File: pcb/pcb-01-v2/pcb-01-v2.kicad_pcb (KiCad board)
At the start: 4 copper layers, 88 x 64 mm, 166 parts, among them J1 43045-0200 POWER, J2 43650-0300, J3 B3B-PH-K-S(LF)(SN), J4 USB4105-GF-A, Q1 DMP6023LE-13, Q2 2N7002K-7, Q3 2N7002K-7, SW1 PTS645SK43SMTR92LFS, SW2 PTS645SK43SMTR92LFS, SW3 PTS645SK43SMTR92LFS, U1 MCF8316DVRGFR, U10 SN74LVC1G17DCKR, U11 SN74LVC1G17DCKR, U12 TMP1075DGKR, U13 TPD2EUSB30DRTR, U14 TPD2EUSB30DRTR, U2 ESP32-C6-WROOM-1-N8, U3 TPSM365R6V3RDNR, U4 TPS7A1601ADGNR, U5 SN74LVC1G74DCTR, U6 SN74LVC1G74DCTR, U7 TPS3435CAKAGDDFR, U8 LM2907M-14/NOPB, U9 TLV1701AIDBVR

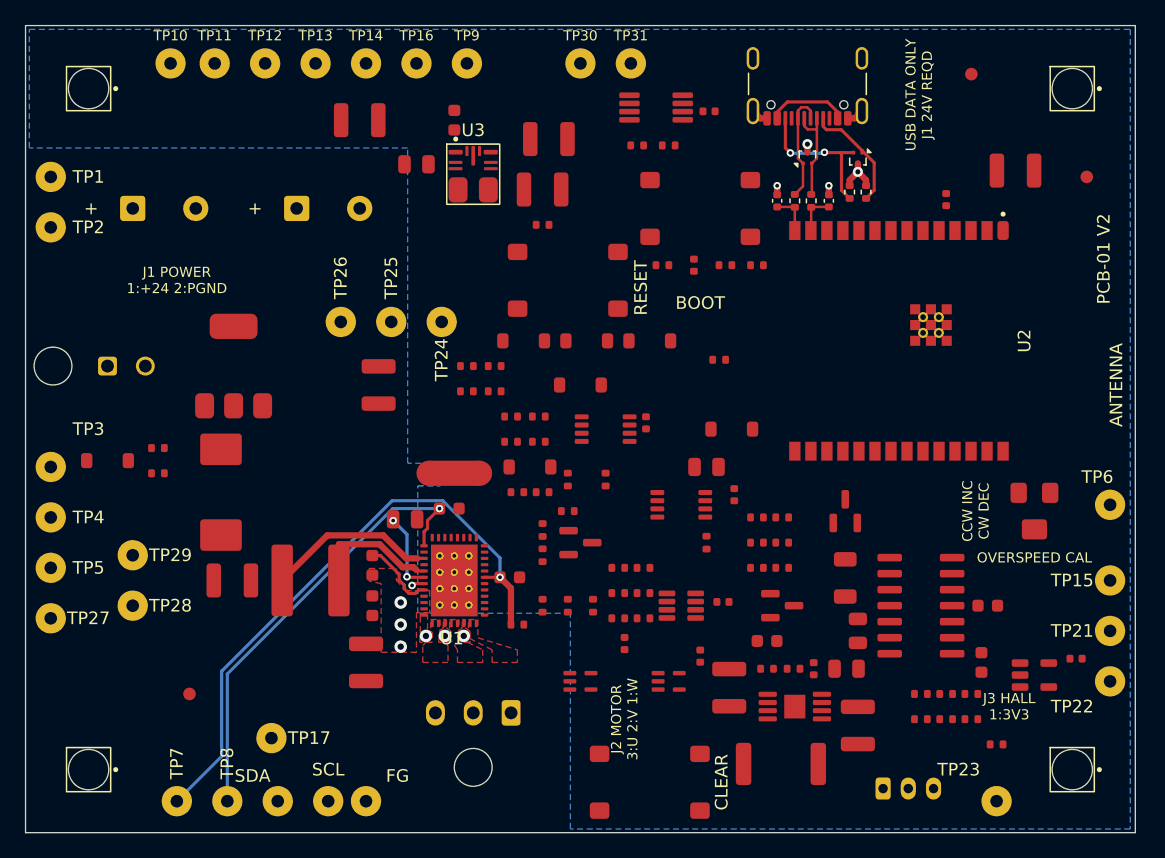
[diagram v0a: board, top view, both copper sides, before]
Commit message: Complete provisional PCB-01 V2 routing
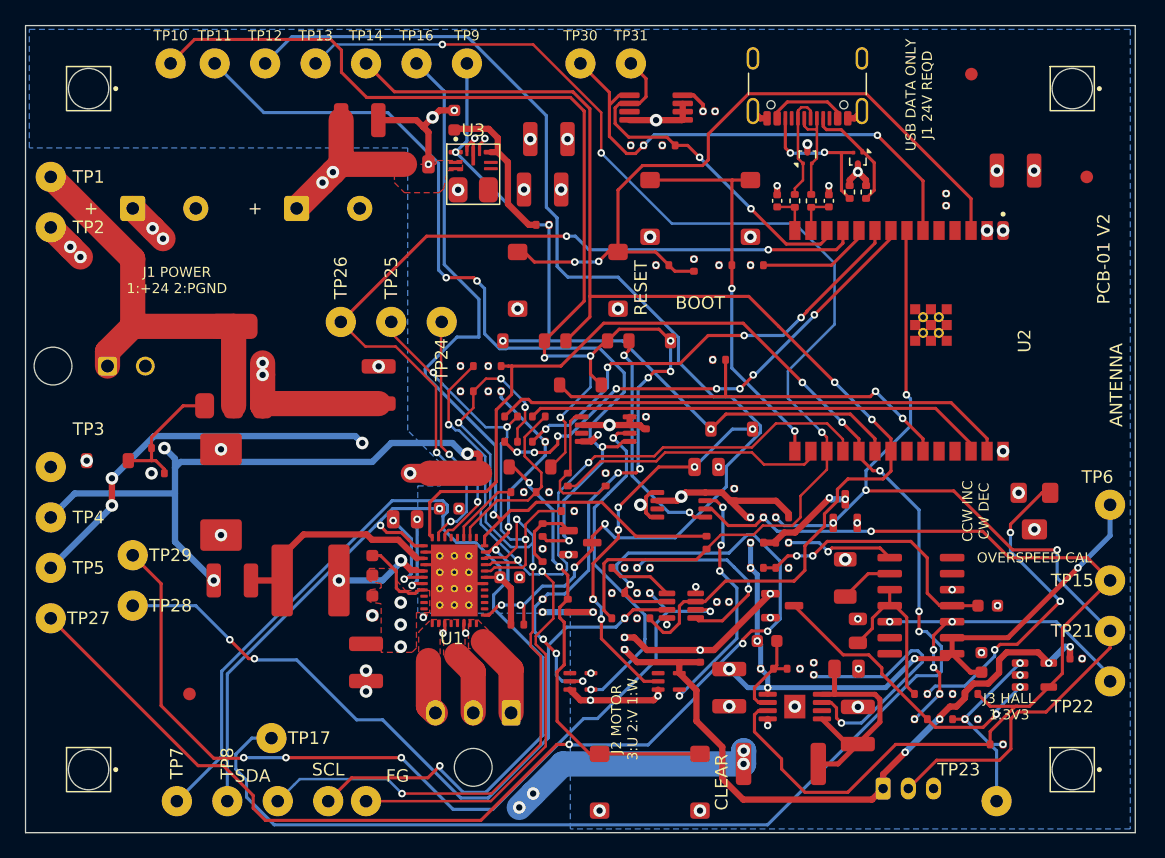
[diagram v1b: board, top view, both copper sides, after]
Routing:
- net NFAULT: track 0.00 -> 142.0 mm, vias 0 -> 5
- net U5_CLR_OR: track 0.00 -> 119.8 mm, vias 0 -> 12
- net 3V3: track 0.00 -> 114.1 mm, vias 0 -> 38
- net AGND: track 8.22 -> 108.4 mm, vias 4 -> 68
- net WD_MR: track 0.00 -> 98.3 mm, vias 0 -> 4
- net WDO: track 0.00 -> 97.5 mm, vias 0 -> 2
- net WD_HEARTBEAT: track 0.00 -> 96.4 mm, vias 0 -> 3
- net DRVOFF: track 0.00 -> 93.8 mm, vias 0 -> 4
- net FG: track 0.00 -> 90.6 mm, vias 0 -> 4
- net OVERSPEED_N: track 0.00 -> 81.4 mm, vias 0 -> 2
- net HALL_TACH: track 0.00 -> 79.5 mm, vias 0 -> 5
- net SDA: track 0.00 -> 73.0 mm, vias 0 -> 6
- net WD_EN: track 0.00 -> 71.3 mm, vias 0 -> 5
- net U5_Q: track 0.00 -> 70.7 mm, vias 0 -> 4
- net ALARM: track 0.00 -> 68.2 mm, vias 0 -> 4
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- removed copper zone on F.Cu, net PGND

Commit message: Finalize PCB-01 V2 JLC submission package
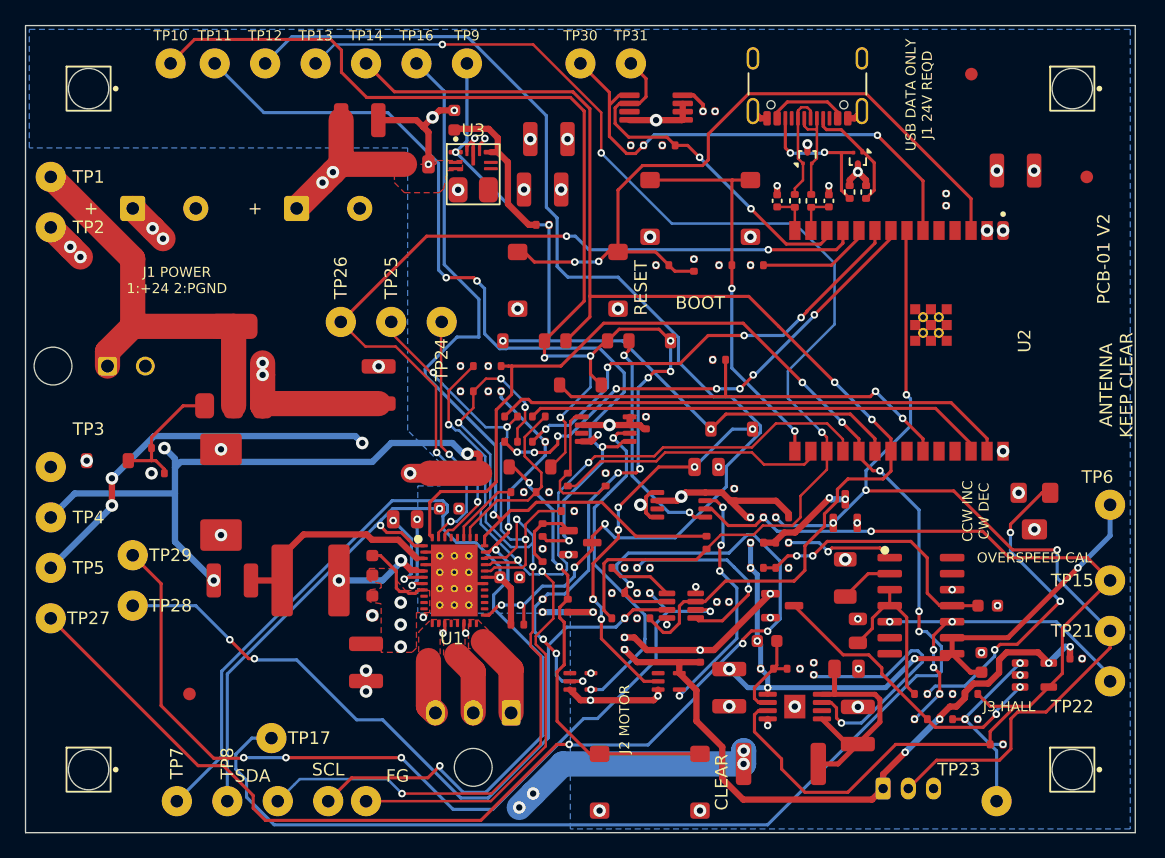
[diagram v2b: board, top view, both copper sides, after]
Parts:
- U8: value LM2907M-14/NOPB -> LM2907M/NOPB
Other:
- board text added: "ANTENNA KEEP CLEAR"
- board text added: "J2 3:U 2:V 1:W"
- board text added: "J2 MOTOR"
- board text added: "J3 HALL"
- board text added: "PHASES: DIFF PROBE ONLY"
- board text added: "STILLAIR"
- board text added: "TP18 SDA"
- board text added: "TP19 SCL"
- board text added: "TP20 FG"
- board text added: "U8 PIN 1"
- board text removed: "ANTENNA"
- board text removed: "J2 MOTOR 3:U 2:V 1:W"
- board text removed: "J3 HALL 1:3V3"
